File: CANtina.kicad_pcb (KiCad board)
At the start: 2 copper layers, 37 x 61.2 mm, 14 parts, among them J1 Screw_Terminal_01x02, J10 Screw_Terminal_01x02, J2 Screw_Terminal_01x02, J3 Screw_Terminal_01x02, J4 Screw_Terminal_01x02, J5 Screw_Terminal_01x02, J6 Screw_Terminal_01x02, J7 Screw_Terminal_01x02, J8 Screw_Terminal_01x02, J9 Screw_Terminal_01x02

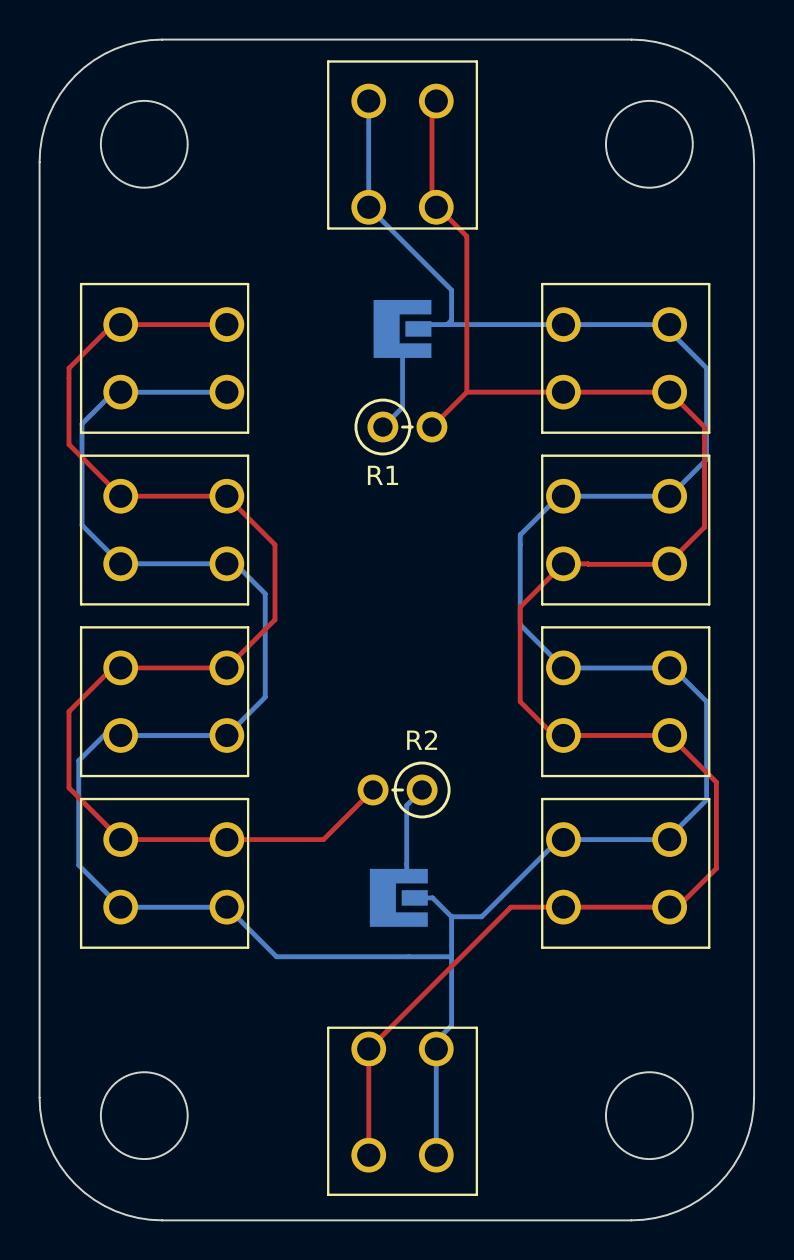
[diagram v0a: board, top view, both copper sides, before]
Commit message: fixed pcb traces
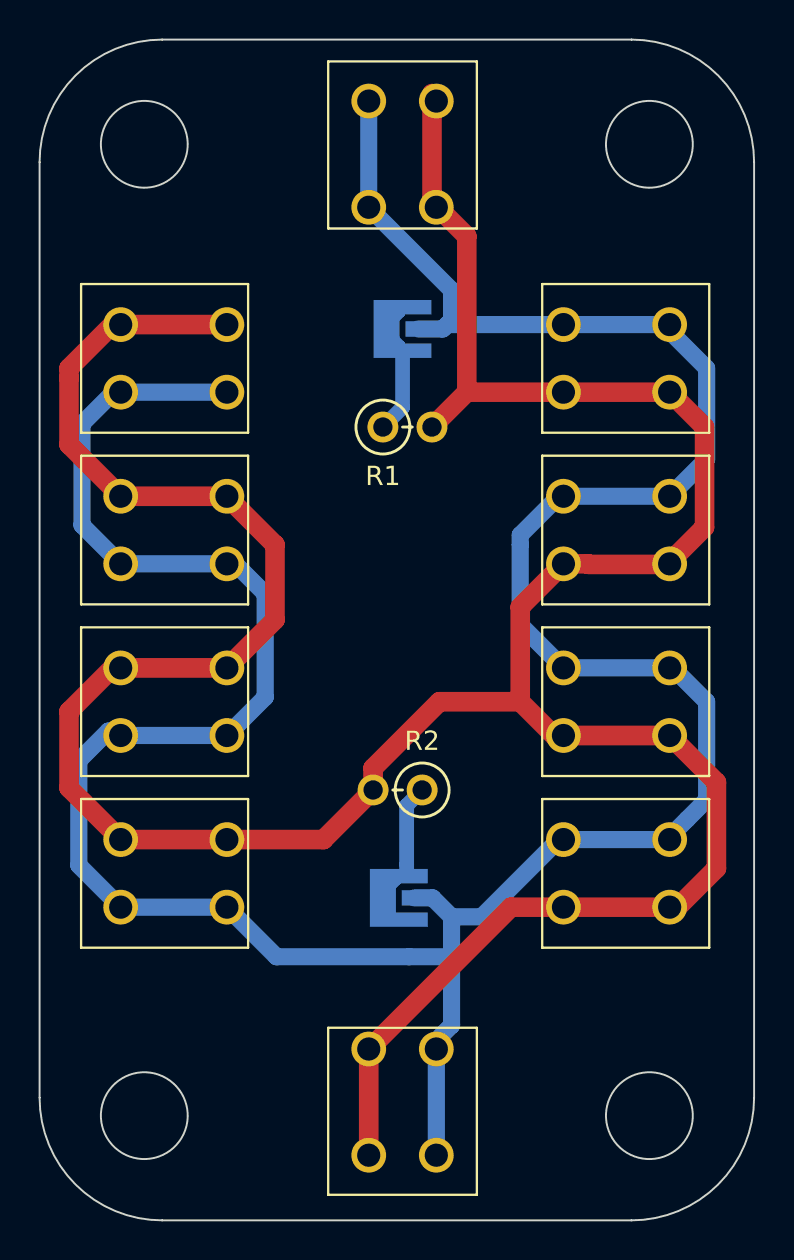
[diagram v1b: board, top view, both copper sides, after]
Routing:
- net Net-(J1-Pad1): track 162.0 -> 172.2 mm
- net Net-(JP1-Pad2): track 4.38 -> 7.66 mm
- net Net-(JP2-Pad2): track 5.02 -> 7.85 mm
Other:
- board text added: "CANtina v1.3 Designed by Zach Brown"
- board text removed: "CANtina v1.2 Designed by Zach Brown"
